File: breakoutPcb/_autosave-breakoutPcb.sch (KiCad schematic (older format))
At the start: 16 parts, among them J1 DB9_Female_MountingHoles, J2 ConY1, J3 ConY2, J4 ConX1, J5 ConX2

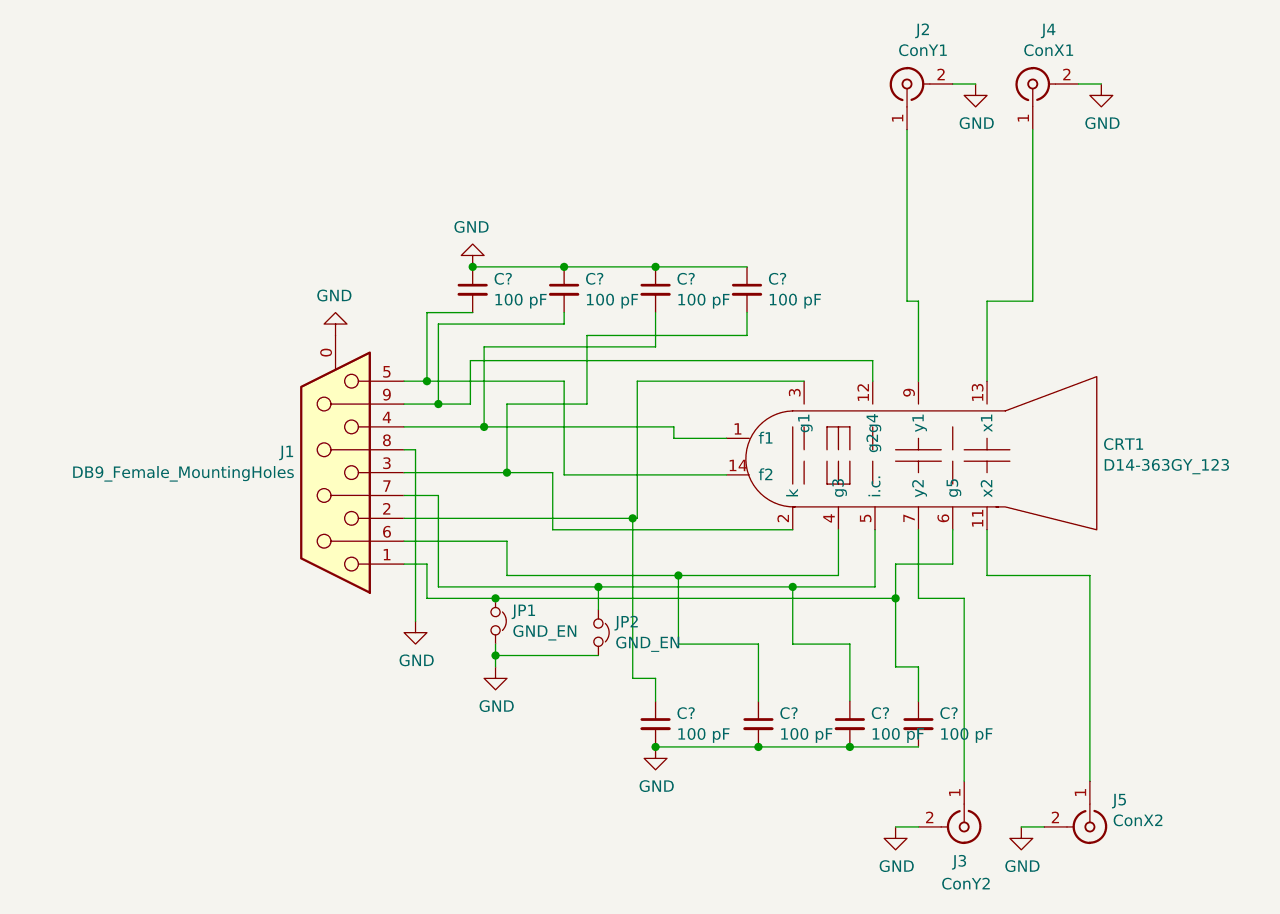
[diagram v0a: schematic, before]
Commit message: Updated layout (no matching, with new decoupling)
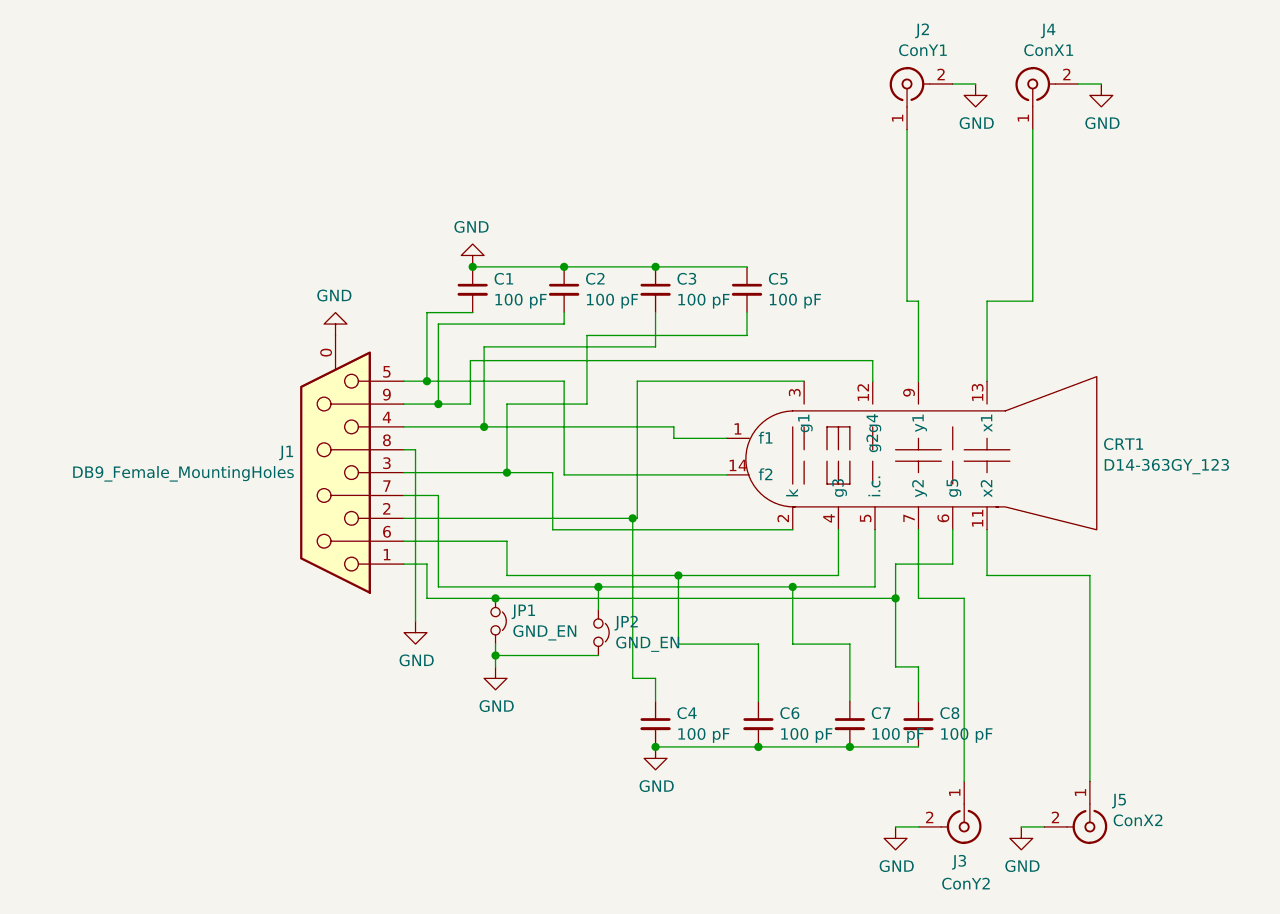
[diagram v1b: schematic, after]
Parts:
- gave numbers to parts that had none: 8
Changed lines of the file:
@@
 	6200 2250 6200 1500
 $Comp
-L power:GND #PWR?
+L power:GND #PWR0101
 U 1 1 626032F2
 P 6150 4550
-F 0 "#PWR?" H 6150 4300 50  0001 C CNN
+F 0 "#PWR0101" H 6150 4300 50  0001 C CNN
 F 1 "GND" H 6155 4377 50  0000 C CNN
 F 2 "" H 6150 4550 50  0001 C CNN
@@
 $EndComp
 $Comp
-L power:GND #PWR?
+L power:GND #PWR0103
 U 1 1 62603766
 P 6500 1300
-F 0 "#PWR?" H 6500 1050 50  0001 C CNN
+F 0 "#PWR0103" H 6500 1050 50  0001 C CNN
 F 1 "GND" H 6505 1127 50  0000 C CNN
 F 2 "" H 6500 1300 50  0001 C CNN
@@
 $EndComp
 $Comp
-L power:GND #PWR?
+L power:GND #PWR0104
 U 1 1 62605013
 P 5950 1300
-F 0 "#PWR?" H 5950 1050 50  0001 C CNN
+F 0 "#PWR0104" H 5950 1050 50  0001 C CNN
 F 1 "GND" H 5955 1127 50  0000 C CNN
 F 2 "" H 5950 1300 50  0001 C CNN
@@
 $EndComp
 $Comp
-L Device:C_Small C?
+L Device:C_Small C1
 U 1 1 62606A14
 P 3750 2200
-F 0 "C?" H 3842 2246 50  0000 L CNN
+F 0 "C1" H 3842 2246 50  0000 L CNN
 F 1 "100 pF" H 3842 2155 50  0000 L CNN
 F 2 "Capacitor_THT:C_Disc_D5.0mm_W2.5mm_P5.00mm" H 3750 2200 50  0001 C CNN
@@
 $EndComp
 $Comp
-L Device:C_Small C?
+L Device:C_Small C2
 U 1 1 6260D1B3
 P 4150 2200
-F 0 "C?" H 4242 2246 50  0000 L CNN
+F 0 "C2" H 4242 2246 50  0000 L CNN
 F 1 "100 pF" H 4242 2155 50  0000 L CNN
 F 2 "Capacitor_THT:C_Disc_D5.0mm_W2.5mm_P5.00mm" H 4150 2200 50  0001 C CNN
@@
 $EndComp
 $Comp
-L Device:C_Small C?
+L Device:C_Small C3
 U 1 1 6260D7AC
 P 4550 2200
-F 0 "C?" H 4642 2246 50  0000 L CNN
+F 0 "C3" H 4642 2246 50  0000 L CNN
 F 1 "100 pF" H 4642 2155 50  0000 L CNN
 F 2 "Capacitor_THT:C_Disc_D5.0mm_W2.5mm_P5.00mm" H 4550 2200 50  0001 C CNN
@@
 $EndComp
 $Comp
-L Device:C_Small C?
+L Device:C_Small C5
 U 1 1 6260DB31
 P 4950 2200
-F 0 "C?" H 5042 2246 50  0000 L CNN
+F 0 "C5" H 5042 2246 50  0000 L CNN
 F 1 "100 pF" H 5042 2155 50  0000 L CNN
 F 2 "Capacitor_THT:C_Disc_D5.0mm_W2.5mm_P5.00mm" H 4950 2200 50  0001 C CNN
@@
 	3900 3000 3450 3000
 $Comp
-L Device:C_Small C?
+L Device:C_Small C4
 U 1 1 626143E3
 P 4550 4100
-F 0 "C?" H 4642 4146 50  0000 L CNN
+F 0 "C4" H 4642 4146 50  0000 L CNN
 F 1 "100 pF" H 4642 4055 50  0000 L CNN
 F 2 "Capacitor_THT:C_Disc_D5.0mm_W2.5mm_P5.00mm" H 4550 4100 50  0001 C CNN
@@
 $EndComp
 $Comp
-L Device:C_Small C?
+L Device:C_Small C6
 U 1 1 62615384
 P 5000 4100
-F 0 "C?" H 5092 4146 50  0000 L CNN
+F 0 "C6" H 5092 4146 50  0000 L CNN
 F 1 "100 pF" H 5092 4055 50  0000 L CNN
 F 2 "Capacitor_THT:C_Disc_D5.0mm_W2.5mm_P5.00mm" H 5000 4100 50  0001 C CNN
@@
 $EndComp
 $Comp
-L Device:C_Small C?
+L Device:C_Small C7
 U 1 1 62615673
 P 5400 4100
-F 0 "C?" H 5492 4146 50  0000 L CNN
+F 0 "C7" H 5492 4146 50  0000 L CNN
 F 1 "100 pF" H 5492 4055 50  0000 L CNN
 F 2 "Capacitor_THT:C_Disc_D5.0mm_W2.5mm_P5.00mm" H 5400 4100 50  0001 C CNN
@@
 	5150 3500 5510 3500
 $Comp
-L Device:C_Small C?
+L Device:C_Small C8
 U 1 1 6261BD38
 P 5700 4100
-F 0 "C?" H 5792 4146 50  0000 L CNN
+F 0 "C8" H 5792 4146 50  0000 L CNN
 F 1 "100 pF" H 5792 4055 50  0000 L CNN
 F 2 "Capacitor_THT:C_Disc_D5.0mm_W2.5mm_P5.00mm" H 5700 4100 50  0001 C CNN
@@
 	5400 4200 5000 4200
 $Comp
-L power:GND #PWR?
+L power:GND #PWR0108
 U 1 1 626259EE
 P 4550 4200
-F 0 "#PWR?" H 4550 3950 50  0001 C CNN
+F 0 "#PWR0108" H 4550 3950 50  0001 C CNN
 F 1 "GND" H 4555 4027 50  0000 C CNN
 F 2 "" H 4550 4200 50  0001 C CNN
@@
 Connection ~ 4550 4200
 $Comp
-L power:GND #PWR?
+L power:GND #PWR0109
 U 1 1 62626073
 P 3750 2100
-F 0 "#PWR?" H 3750 1850 50  0001 C CNN
+F 0 "#PWR0109" H 3750 1850 50  0001 C CNN
 F 1 "GND" H 3755 1927 50  0000 C CNN
 F 2 "" H 3750 2100 50  0001 C CNN
